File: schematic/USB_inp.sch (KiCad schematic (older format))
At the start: 10 parts, among them CON1 USB-MICRO-B, Q1 DTA114Y, U4 USBLC6-2

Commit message: PCB
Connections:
- net +3.3V is gone; now on net USB_+5V: C12.2, Q1.2 (E), U4.5 (VBUS)
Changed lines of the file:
@@
-EESchema Schematic File Version 2  date Ср 09 июл 2014 18:42:33
+EESchema Schematic File Version 2  date Пт 11 июл 2014 12:31:03
 LIBS:power
 LIBS:device
@@
 Sheet 4 12
 Title "USB input circuit"
-Date "9 jul 2014"
+Date "11 jul 2014"
 Rev ""
 Comp "SAO RAS"
@@
 Comment4 ""
 $EndDescr
-Wire Wire Line
-	1150 3250 1150 4150
-Connection ~ 1150 3400
-Connection ~ 1150 3700
 Text HLabel 1250 1550 0    60   Input ~ 0
 GND
 $Comp
-L GND #PWR078
+L GND #PWR077
 U 1 1 53983179
 P 1300 1700
-F 0 "#PWR078" H 1300 1700 30  0001 C CNN
+F 0 "#PWR077" H 1300 1700 30  0001 C CNN
 F 1 "GND" H 1300 1630 30  0001 C CNN
 F 2 "" H 1300 1700 60  0000 C CNN
@@
 	1    0    0    -1
 $EndComp
-Wire Wire Line
-	1250 1550 1300 1550
-Wire Wire Line
-	1300 1550 1300 1700
-$Comp
-L GND #PWR079
+$Comp
+L GND #PWR078
 U 1 1 5398318A
 P 1650 4200
-F 0 "#PWR079" H 1650 4200 30  0001 C CNN
+F 0 "#PWR078" H 1650 4200 30  0001 C CNN
 F 1 "GND" H 1650 4130 30  0001 C CNN
 F 2 "" H 1650 4200 60  0000 C CNN
@@
 	1    0    0    -1
 $EndComp
-Connection ~ 1150 3850
-Wire Wire Line
-	1150 4150 2250 4150
-Wire Wire Line
-	1650 4150 1650 4200
-Wire Wire Line
-	2250 4150 2250 3700
-Connection ~ 1650 4150
-Connection ~ 2250 3850
 $Comp
 L USBLC6-2 U4
@@
 	-1   0    0    1
 $EndComp
-Wire Wire Line
-	2250 3400 2800 3400
-Wire Wire Line
-	2250 3550 2800 3550
-Wire Wire Line
-	2800 3550 2800 3500
-Text HLabel 1250 2000 0    60   Input ~ 0
-+3.3V
-Wire Wire Line
-	1250 2000 1350 2000
-$Comp
-L +3.3V #PWR080
-U 1 1 5395CBF8
-P 1350 2000
-F 0 "#PWR080" H 1350 1960 30  0001 C CNN
-F 1 "+3.3V" H 1350 2110 30  0000 C CNN
-F 2 "" H 1350 2000 60  0000 C CNN
-F 3 "" H 1350 2000 60  0000 C CNN
-	1    1350 2000
-	1    0    0    -1
-$EndComp
 Text HLabel 5850 3250 2    60   Output ~ 0
 USB_POWER
@@
 	1    0    0    -1
 $EndComp
-Wire Wire Line
-	2250 3000 2250 3250
 $Comp
 L R R7
@@
 	1    0    0    -1
 $EndComp
-Wire Wire Line
-	1250 2250 2250 2250
-Wire Wire Line
-	2250 2250 2250 2500
-Connection ~ 1450 2250
-$Comp
-L GND #PWR081
+$Comp
+L GND #PWR079
 U 1 1 5395CECD
 P 1450 2850
-F 0 "#PWR081" H 1450 2850 30  0001 C CNN
+F 0 "#PWR079" H 1450 2850 30  0001 C CNN
 F 1 "GND" H 1450 2780 30  0001 C CNN
 F 2 "" H 1450 2850 60  0000 C CNN
@@
 	1    0    0    -1
 $EndComp
-Wire Wire Line
-	1450 2850 1450 2750
 $Comp
 L R R9
@@
 	1    0    0    -1
 $EndComp
-Wire Wire Line
-	5200 2500 5200 2400
-$Comp
-L +3.3V #PWR082
-U 1 1 5395D1C1
-P 5200 1850
-F 0 "#PWR082" H 5200 1810 30  0001 C CNN
-F 1 "+3.3V" H 5200 1960 30  0000 C CNN
-F 2 "" H 5200 1850 60  0000 C CNN
-F 3 "" H 5200 1850 60  0000 C CNN
-	1    5200 1850
-	1    0    0    -1
-$EndComp
-Wire Wire Line
-	5200 1850 5200 2000
-Wire Wire Line
-	5200 3000 5200 3550
 Text HLabel 5850 3100 2    60   Input ~ 0
 USB_DISC
 $Comp
-L GND #PWR083
+L GND #PWR080
 U 1 1 5395D488
 P 2650 3250
-F 0 "#PWR083" H 2650 3250 30  0001 C CNN
+F 0 "#PWR080" H 2650 3250 30  0001 C CNN
 F 1 "GND" H 2650 3180 30  0001 C CNN
 F 2 "" H 2650 3250 60  0000 C CNN
@@
 	1    0    0    -1
 $EndComp
-Wire Wire Line
-	2650 3250 2650 3150
-Wire Wire Line
-	2650 3150 2800 3150
-Wire Wire Line
-	2800 3100 2800 3300
-$Comp
-L +3.3V #PWR084
-U 1 1 5395D4AB
-P 3900 3100
-F 0 "#PWR084" H 3900 3060 30  0001 C CNN
-F 1 "+3.3V" H 3900 3210 30  0000 C CNN
-F 2 "" H 3900 3100 60  0000 C CNN
-F 3 "" H 3900 3100 60  0000 C CNN
-	1    3900 3100
-	1    0    0    -1
-$EndComp
-Wire Wire Line
-	3900 3100 3900 3300
-Wire Wire Line
-	4500 3400 5850 3400
 Text Label 1250 2250 0    60   ~ 0
 USB_POWER
 Text Label 5750 3250 2    60   ~ 0
 USB_POWER
-Wire Wire Line
-	5750 3250 5850 3250
 Text HLabel 5850 3550 2    60   BiDi ~ 0
 USB_DP
 Text HLabel 5850 3400 2    60   BiDi ~ 0
 USB_DM
-Wire Wire Line
-	4500 3550 5850 3550
 $Comp
 L C C12
@@
 	0    -1   -1   0
 $EndComp
-Wire Wire Line
-	3550 3100 3900 3100
-Wire Wire Line
-	2800 3100 3150 3100
-Connection ~ 2800 3150
-Wire Wire Line
-	5750 3100 5850 3100
-Wire Wire Line
-	5550 2200 5750 2200
-Wire Wire Line
-	5750 2200 5750 3100
 $Comp
 L R R35
@@
 	0    -1   -1   0
 $EndComp
-Wire Wire Line
-	3900 3400 4000 3400
-Wire Wire Line
-	3900 3500 4000 3500
-Wire Wire Line
-	4000 3500 4000 3550
-Connection ~ 5200 3550
 $Comp
 L DIODESCH D3
@@
 	0    -1   -1   0
 $EndComp
-Wire Wire Line
-	2250 3100 2500 3100
-Wire Wire Line
-	2500 3100 2500 2950
-Connection ~ 2250 3100
-Wire Wire Line
-	2500 2550 2500 2450
 Text Label 2500 2450 0    60   ~ 0
 USB_+5V
 Text Label 5750 3750 2    60   ~ 0
 USB_+5V
-Wire Wire Line
-	5750 3750 5850 3750
 Text HLabel 5850 3750 2    61   Output ~ 0
 USB_+5V
@@
 	-1   0    0    -1
 $EndComp
+Wire Wire Line
+	1150 3250 1150 4150
+Connection ~ 1150 3400
+Connection ~ 1150 3700
+Wire Wire Line
+	1250 1550 1300 1550
+Wire Wire Line
+	1300 1550 1300 1700
+Connection ~ 1150 3850
+Wire Wire Line
+	1150 4150 2250 4150
+Wire Wire Line
+	1650 4150 1650 4200
+Wire Wire Line
+	2250 4150 2250 3700
+Connection ~ 1650 4150
+Connection ~ 2250 3850
+Wire Wire Line
+	2250 3400 2800 3400
+Wire Wire Line
+	2250 3550 2800 3550
+Wire Wire Line
+	2800 3550 2800 3500
+Wire Wire Line
+	2250 3000 2250 3250
+Wire Wire Line
+	1250 2250 2250 2250
+Wire Wire Line
+	2250 2250 2250 2500
+Connection ~ 1450 2250
+Wire Wire Line
+	1450 2850 1450 2750
+Wire Wire Line
+	5200 2500 5200 2400
+Wire Wire Line
+	5200 3000 5200 3550
+Wire Wire Line
+	2650 3250 2650 3150
+Wire Wire Line
+	2650 3150 2800 3150
+Wire Wire Line
+	2800 3100 2800 3300
+Wire Wire Line
+	4500 3400 5850 3400
+Wire Wire Line
+	5750 3250 5850 3250
+Wire Wire Line
+	4500 3550 5850 3550
+Wire Wire Line
+	3550 3100 3900 3100
+Wire Wire Line
+	2800 3100 3150 3100
+Connection ~ 2800 3150
+Wire Wire Line
+	5750 3100 5850 3100
+Wire Wire Line
+	5550 2200 5750 2200
+Wire Wire Line
+	5750 2200 5750 3100
+Wire Wire Line
+	3900 3400 4000 3400
+Wire Wire Line
+	3900 3500 4000 3500
+Wire Wire Line
+	4000 3500 4000 3550
+Connection ~ 5200 3550
+Wire Wire Line
+	2250 3100 2500 3100
+Wire Wire Line
+	2500 3100 2500 2950
+Connection ~ 2250 3100
+Wire Wire Line
+	2500 2550 2500 2450
+Wire Wire Line
+	5750 3750 5850 3750
+Wire Wire Line
+	3900 2500 2500 2500
+Connection ~ 2500 2500
+Connection ~ 3900 2500
+Wire Wire Line
+	5200 2000 3900 2000
+Wire Wire Line
+	3900 2000 3900 3300
+Connection ~ 3900 3100
 $EndSCHEMATC

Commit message: last?
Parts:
- CON1: footprint MICRO-B-USB -> MINI-B-USB
- renumbered U4 to DA4, D3 to VD3, Q1 to VT1
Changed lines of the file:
@@
-EESchema Schematic File Version 2  date Пт 11 июл 2014 12:31:03
+EESchema Schematic File Version 2  date Пт 18 июл 2014 12:36:52
 LIBS:power
 LIBS:device
@@
 Sheet 4 12
 Title "USB input circuit"
-Date "11 jul 2014"
+Date "18 jul 2014"
 Rev ""
 Comp "SAO RAS"
@@
 GND
 $Comp
-L GND #PWR077
+L GND #PWR075
 U 1 1 53983179
 P 1300 1700
-F 0 "#PWR077" H 1300 1700 30  0001 C CNN
+F 0 "#PWR075" H 1300 1700 30  0001 C CNN
 F 1 "GND" H 1300 1630 30  0001 C CNN
 F 2 "" H 1300 1700 60  0000 C CNN
@@
 $EndComp
 $Comp
-L GND #PWR078
+L GND #PWR076
 U 1 1 5398318A
 P 1650 4200
-F 0 "#PWR078" H 1650 4200 30  0001 C CNN
+F 0 "#PWR076" H 1650 4200 30  0001 C CNN
 F 1 "GND" H 1650 4130 30  0001 C CNN
 F 2 "" H 1650 4200 60  0000 C CNN
@@
 $EndComp
 $Comp
-L USBLC6-2 U4
+L USBLC6-2 DA4
 U 1 1 5395C045
 P 3350 3400
-F 0 "U4" H 3200 3100 60  0000 C CNN
+F 0 "DA4" H 3200 3100 60  0000 C CNN
 F 1 "USBLC6-2" H 3350 3200 60  0000 C CNN
 F 2 "SOT23_6" H 3350 3400 60  0001 C CNN
@@
 $EndComp
 $Comp
-L DTA114Y Q1
+L DTA114Y VT1
 U 1 1 5395C059
 P 5300 2200
-F 0 "Q1" H 5245 2040 40  0000 R CNN
+F 0 "VT1" H 5245 2040 40  0000 R CNN
 F 1 "DTA114Y" H 5300 2350 40  0000 R CNN
 F 2 "SOT323" H 5300 2200 60  0001 C CNN
@@
 $EndComp
 $Comp
-L GND #PWR079
+L GND #PWR077
 U 1 1 5395CECD
 P 1450 2850
-F 0 "#PWR079" H 1450 2850 30  0001 C CNN
+F 0 "#PWR077" H 1450 2850 30  0001 C CNN
 F 1 "GND" H 1450 2780 30  0001 C CNN
 F 2 "" H 1450 2850 60  0000 C CNN
@@
 USB_DISC
 $Comp
-L GND #PWR080
+L GND #PWR078
 U 1 1 5395D488
 P 2650 3250
-F 0 "#PWR080" H 2650 3250 30  0001 C CNN
+F 0 "#PWR078" H 2650 3250 30  0001 C CNN
 F 1 "GND" H 2650 3180 30  0001 C CNN
 F 2 "" H 2650 3250 60  0000 C CNN
@@
 $EndComp
 $Comp
-L DIODESCH D3
+L DIODESCH VD3
 U 1 1 539B75AF
 P 2500 2750
-F 0 "D3" H 2500 2850 40  0000 C CNN
+F 0 "VD3" H 2500 2850 40  0000 C CNN
 F 1 "B120-E3" H 2500 2650 40  0000 C CNN
 F 2 "DO-214" H 2500 2750 60  0001 C CNN
@@
 F 0 "CON1" H 1450 4000 60  0000 C CNN
 F 1 "USB-MICRO-B" H 1650 3050 60  0000 C CNN
-F 2 "MICRO-B-USB" H 1700 3550 60  0001 C CNN
+F 2 "MINI-B-USB" H 1700 3550 60  0001 C CNN
 F 3 "~" H 1700 3550 60  0000 C CNN
 	1    1700 3550

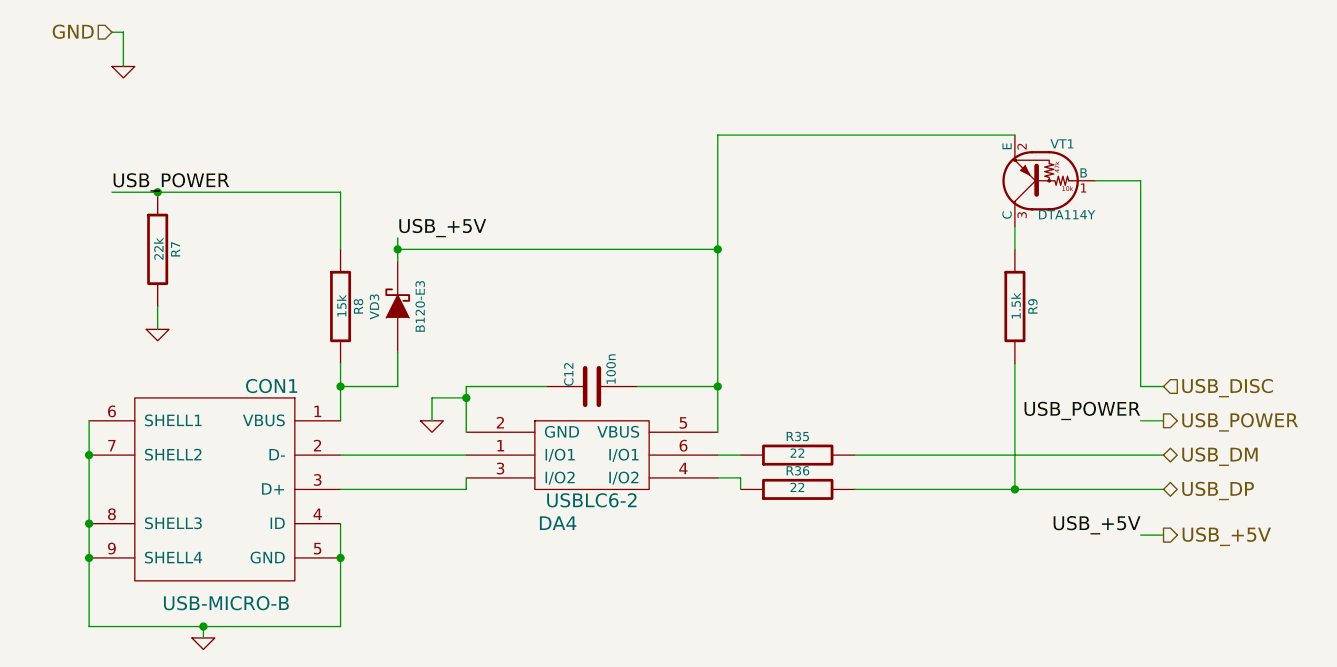
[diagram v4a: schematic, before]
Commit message: try to make 1-wire on timers
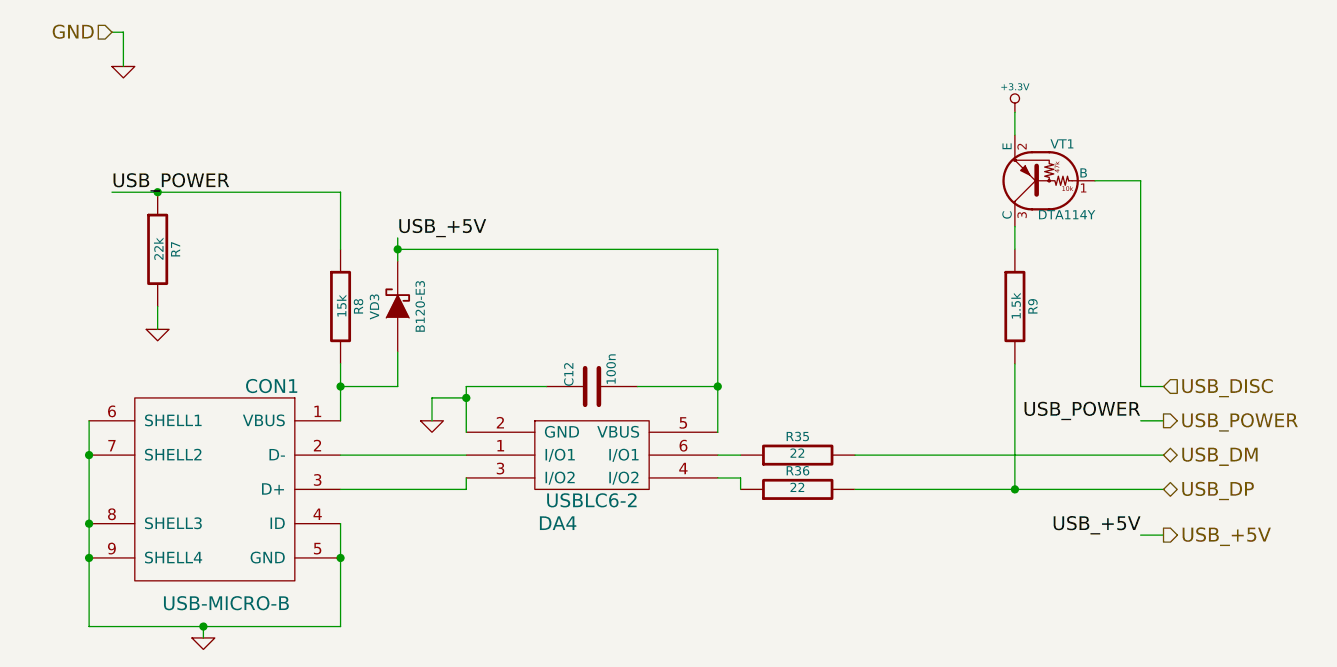
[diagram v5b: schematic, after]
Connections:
- net USB_+5V: no longer VT1.2 (E)
- new net +3.3V: VT1.2 (E)
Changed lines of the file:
@@
-EESchema Schematic File Version 2  date Пн 29 сен 2014 14:40:29
+EESchema Schematic File Version 2  date Вт 07 окт 2014 17:18:47
 LIBS:power
 LIBS:device
@@
 Sheet 4 12
 Title "USB input circuit"
-Date "29 sep 2014"
+Date "7 oct 2014"
 Rev ""
 Comp "SAO RAS"
@@
 	3900 2500 2500 2500
 Connection ~ 2500 2500
-Connection ~ 3900 2500
-Wire Wire Line
-	5200 2000 3900 2000
-Wire Wire Line
-	3900 2000 3900 3300
 Connection ~ 3900 3100
+Wire Wire Line
+	3900 3300 3900 2500
+$Comp
+L +3.3V #PWR?
+U 1 1 5433F723
+P 5200 1900
+F 0 "#PWR?" H 5200 1860 30  0001 C CNN
+F 1 "+3.3V" H 5200 2010 30  0000 C CNN
+F 2 "" H 5200 1900 60  0000 C CNN
+F 3 "" H 5200 1900 60  0000 C CNN
+	1    5200 1900
+	1    0    0    -1
+$EndComp
+Wire Wire Line
+	5200 1900 5200 2000
 $EndSCHEMATC
